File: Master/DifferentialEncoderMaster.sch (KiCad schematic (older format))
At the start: 52 parts, among them J1 RJ45_Shielded, J10 Conn_02x06_Top_Bottom, J11 Conn_02x06_Top_Bottom, J12 CAN_Header, J13 Conn_02x04_Top_Bottom, J2 Conn_01x06, J3 Conn_01x20, J4 Conn_01x12, J5 RJ45_Shielded, J6 RJ45_Shielded, J7 RJ45_Shielded, J8 Jumper, J9 Jumper, U1 SN75C1167, U2 SN75C1167, U3 ST26C32ABTR, U4 ST26C32ABTR, U5 ISO7760FDBQ, U6 ISO7761DBQ

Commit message: Big updates to master
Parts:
- removed J1, J5, J6, J7: RJ45_Shielded, Connector_RJ:RJ45_Amphenol_RJHSE538X, symbol Connector:RJ45_Shielded
- removed U5: ISO7760FDBQ, Package_SO:SSOP-16_3.9x4.9mm_P0.635mm, symbol Isolator:ISO7760FDBQ
- added C10, C11: 100nF, Capacitor_SMD:C_0603_1608Metric, symbol Device:C_Small
- added J1, J5: RJ45_Shielded_x2, Wetmelon:RJ45_RJSSE5380-02, symbol Wetmelon:RJ45_Shielded_x2
- added R19, R20: 0R, Resistor_SMD:R_0603_1608Metric, symbol Device:R_Small
- FB1, FB2: footprint (none) -> Inductor_SMD:L_0603_1608Metric
- J10: value Conn_02x06_Top_Bottom -> Encoder_0
- J11: value Conn_02x06_Top_Bottom -> Encoder_1
- J13: value Conn_02x04_Top_Bottom -> ISO_GPIO; footprint (none) -> Connector_Molex:Molex_Nano-Fit_105310-xx08_2x04_P2.50mm_Vertical
- J8, J9: footprint (none) -> Connector_PinHeader_2.54mm:PinHeader_1x02_P2.54mm_Vertical
- R17, R18: footprint (none) -> Resistor_SMD:R_0603_1608Metric
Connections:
- net IO_M0_A is gone; now on net M0_A: J10.2 (Pin_2), J10.4 (Pin_4), U3.3 (A_Out)
- net IO_M0_B is gone; now on net M0_B: J10.10 (Pin_10), J10.8 (Pin_8), U3.5 (B_Out)
- net IO_M0_Z is gone; now on net M0_Z: J10.11 (Pin_11), J10.7 (Pin_7), U3.11 (C_Out)
- net IO_M1_A is gone; now on net M1_A: J11.2 (Pin_2), J11.4 (Pin_4), U4.3 (A_Out)
- net IO_M1_B is gone; now on net M1_B: J11.10 (Pin_10), J11.8 (Pin_8), U4.5 (B_Out)
- net IO_M1_Z is gone; now on net M1_Z: J11.11 (Pin_11), J11.7 (Pin_7), U4.11 (C_Out)
- net +5V: now also C6.1, J10.1 (Pin_1), J10.5 (Pin_5), J11.1 (Pin_1), J11.5 (Pin_5), R17.2, R18.2, U3.16 (Vcc), U4.16 (Vcc), C10.1, C11.1, J1.15, J1.7, J5.15, J5.7
- net CLK_1+: now also J1.3
- net CLK_1-: now also J1.6
- net CLK_2+: now also J1.11
- net CLK_2-: now also J1.14
- net CSn_1: now also R19.1; no longer U1.4 (~RE)
- net CSn_1+: now also J1.1
- net CSn_1-: now also J1.2
- net CSn_2: now also R20.1; no longer U2.4 (~RE)
- net CSn_2+: now also J1.9
- net CSn_2-: now also J1.10
- net ENC0_A+: now also J5.1
- net ENC0_A-: now also J5.2
- net ENC0_B+: now also J5.3
- net ENC0_B-: now also J5.6
- net ENC0_Z+: now also J5.5
- net ENC0_Z-: now also J5.4
- net ENC1_A+: now also J5.9
- net ENC1_A-: now also J5.10
- net ENC1_B+: now also J5.11
- net ENC1_B-: now also J5.14
- net ENC1_Z+: now also J5.13
- net ENC1_Z-: now also J5.12
- net GNDD: now also C6.2, J8.2 (Pin_2), J9.2 (Pin_2), U3.4 (EN), U3.8 (GND), U4.4 (EN), U4.8 (GND), C10.2, C11.2, J1.16, J1.8, J1.SH, J1.SH, J5.16, J5.8, J5.SH, J5.SH
- net GPIO5: no longer J10.6 (Pin_6)
- net GPIO6: no longer J11.6 (Pin_6)
- net ISO_DIR_1: now also J13.3 (Pin_3), U6.3 (INB); no longer J13.4 (Pin_4), U6.4 (INC)
- net ISO_DIR_2: now also J13.7 (Pin_7); no longer J13.8 (Pin_8)
- net ISO_STEP_1: now also J13.4 (Pin_4); no longer J13.3 (Pin_3)
- net ISO_STEP_2: now also J13.8 (Pin_8), U6.4 (INC); no longer J13.7 (Pin_7), U6.3 (INB)
- net MISO_1+: now also J1.5
- net MISO_1-: now also J1.4
- net MISO_2+: now also J1.13
- net MISO_2-: now also J1.12
- removed net AGND: J10.12 (Pin_12), J11.12 (Pin_12), J3.7 (Pin_7)
- net AVCC: no longer names the net of J3.6 (Pin_6)
- removed net GND2: C6.2, C7.2, FB2.1, J13.2 (Pin_2), J8.2 (Pin_2), J9.2 (Pin_2), U3.4 (EN), U3.8 (GND), U4.4 (EN), U4.8 (GND), U6.8 (GND1)
- net MOSI: no longer names the net of J3.10 (Pin_10)
- net SWC: no longer names the net of J2.3 (Pin_3)
- net SWD: no longer names the net of J2.5 (Pin_5)
- removed net VDD: C6.1, C7.1, FB1.1, J10.1 (Pin_1), J10.5 (Pin_5), J11.1 (Pin_1), J11.5 (Pin_5), J13.1 (Pin_1), R17.2, R18.2, U3.16 (Vcc), U4.16 (Vcc), U6.1 (Vcc1)
- net ~RST: no longer names the net of J2.6 (Pin_6)
- new net: R19.2, U1.4 (~RE)
- new net: R20.2, U2.4 (~RE)
- new net GND1: C7.2, FB2.1, J13.2 (Pin_2), U6.8 (GND1)
- new net VDD1: C7.1, FB1.1, J13.1 (Pin_1), U6.1 (Vcc1)
- no-connect marks 12 -> 22
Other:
- note added: "AGND"
- note added: "AVCC"
- note added: "MOSI"
- note added: "RC Filters for Single-Ended SPI Signals\n10.6 MHz"
- note added: "SWC"
- note added: "SWD"
- note added: "~RST"
- note removed: "Incremental Encoder Isolator"
- note removed: "RC Filters for Single-Ended SPI Signals"
- moved on the sheet: C5, C7, C9, FB1, FB2, J10, J11, J12, J13, J2, J3, J4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

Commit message: Finish rev 1 layout
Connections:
- net ENC0_A+: now also J5.9; no longer J5.1
- net ENC0_A-: now also J5.10; no longer J5.2
- net ENC0_B+: now also J5.11; no longer J5.3
- net ENC0_B-: now also J5.14; no longer J5.6
- net ENC0_Z+: now also J5.13; no longer J5.5
- net ENC0_Z-: now also J5.12; no longer J5.4
- net ENC1_A+: now also J5.1; no longer J5.9
- net ENC1_A-: now also J5.2; no longer J5.10
- net ENC1_B+: now also J5.3; no longer J5.11
- net ENC1_B-: now also J5.6; no longer J5.14
- net ENC1_Z+: now also J5.5; no longer J5.13
- net ENC1_Z-: now also J5.4; no longer J5.12
- net GND1: now also J13.7 (Pin_7); no longer J13.2 (Pin_2)
- net ISO_DIR_1: now also J13.6 (Pin_6); no longer J13.3 (Pin_3)
- net ISO_DIR_2: now also J13.2 (Pin_2); no longer J13.7 (Pin_7)
- net ISO_STEP_1: now also J13.5 (Pin_5); no longer J13.4 (Pin_4)
- net ISO_STEP_2: now also J13.1 (Pin_1); no longer J13.8 (Pin_8)
- net ISO_UART_RX: now also J13.3 (Pin_3); no longer J13.6 (Pin_6)
- net ISO_UART_TX: now also J13.4 (Pin_4); no longer J13.5 (Pin_5)
- net VDD1: now also J13.8 (Pin_8); no longer J13.1 (Pin_1)
- removed net +3.3V: J2.2 (Pin_2), J3.1 (Pin_1), J4.1 (Pin_1), J4.7 (Pin_7)
- no-connect marks 22 -> 26
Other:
- note added: "+3.3V"
- moved on the sheet: J5A, J5B
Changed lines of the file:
@@
 Text Label 12400 5200 2    50   ~ 0
 GPIO8
-$Comp
-L Connector_Generic:Conn_02x04_Top_Bottom J13
-U 1 1 60674364
-P 11500 6900
-F 0 "J13" H 11550 7217 50  0000 C CNN
-F 1 "ISO_GPIO" H 11550 7126 50  0000 C CNN
-F 2 "Connector_Molex:Molex_Nano-Fit_105310-xx08_2x04_P2.50mm_Vertical" H 11500 6900 50  0001 C CNN
-F 3 "~" H 11500 6900 50  0001 C CNN
-	1    11500 6900
-	1    0    0    -1
-$EndComp
-Wire Wire Line
-	10800 6800 11300 6800
 Text Label 10800 6900 0    50   ~ 0
 GND1
-Wire Wire Line
-	10800 6900 11300 6900
 Text Label 10800 7100 0    50   ~ 0
 ISO_STEP_1
-Wire Wire Line
-	10800 7000 11300 7000
 Text Label 10800 7000 0    50   ~ 0
 ISO_DIR_1
-Wire Wire Line
-	10800 7100 11300 7100
 Text Label 12400 6800 2    50   ~ 0
 ISO_UART_TX
@@
 	14550 4700 14850 4700
 Wire Wire Line
-	14550 4600 14850 4600
-Wire Wire Line
 	14550 4500 14850 4500
 Wire Wire Line
@@
 Wire Wire Line
 	14550 4100 14850 4100
-Wire Wire Line
-	14550 4000 14850 4000
 Text Label 14550 5100 0    50   ~ 0
 GNDD
@@
 Text Label 14550 4700 0    50   ~ 0
 +5V
-Text Label 14550 4600 0    50   ~ 0
-+3.3V
 Text Label 14550 4500 0    50   ~ 0
 GNDD
@@
 Text Label 14550 4100 0    50   ~ 0
 +5V
-Text Label 14550 4000 0    50   ~ 0
-+3.3V
 $Comp
 L Connector_Generic:Conn_01x12 J4
@@
 Text Label 13250 4100 0    50   ~ 0
 GNDD
-Text Label 13250 4000 0    50   ~ 0
-+3.3V
-Wire Wire Line
-	13600 4000 13250 4000
 $Comp
 L Connector_Generic:Conn_01x20 J3
@@
 Text Label 14500 5400 0    50   ~ 0
 +5V
-Text Label 14500 5500 0    50   ~ 0
-+3.3V
 Text Label 14500 5700 0    50   ~ 0
 GNDD
 Wire Wire Line
 	14500 5400 14850 5400
-Wire Wire Line
-	14500 5500 14850 5500
 Wire Wire Line
 	14500 5700 14850 5700
@@
 L Wetmelon:RJ45_Shielded_x2 J5
 U 1 1 5FB86974
+P 6550 5200
+F 0 "J5" H 6607 5867 50  0000 C CNN
+F 1 "RJ45_Shielded_x2" H 6607 5776 50  0000 C CNN
+F 2 "Wetmelon:RJ45_RJSSE5380-02" V 6550 5225 50  0001 C CNN
+F 3 "~" V 6550 5225 50  0001 C CNN
+	1    6550 5200
+	-1   0    0    -1
+$EndComp
+$Comp
+L Wetmelon:RJ45_Shielded_x2 J5
+U 2 1 5FB876DB
 P 6550 2550
 F 0 "J5" H 6607 3217 50  0000 C CNN
@@
 F 2 "Wetmelon:RJ45_RJSSE5380-02" V 6550 2575 50  0001 C CNN
 F 3 "~" V 6550 2575 50  0001 C CNN
-	1    6550 2550
-	-1   0    0    -1
-$EndComp
-$Comp
-L Wetmelon:RJ45_Shielded_x2 J5
-U 2 1 5FB876DB
-P 6550 5200
-F 0 "J5" H 6607 5867 50  0000 C CNN
-F 1 "RJ45_Shielded_x2" H 6607 5776 50  0000 C CNN
-F 2 "Wetmelon:RJ45_RJSSE5380-02" V 6550 5225 50  0001 C CNN
-F 3 "~" V 6550 5225 50  0001 C CNN
-	2    6550 5200
+	2    6550 2550
 	-1   0    0    -1
 $EndComp
@@
 Text Label 10500 4900 0    50   ~ 0
 ISO_STEP_1
+Wire Wire Line
+	10800 7100 11300 7100
+Wire Wire Line
+	10800 6800 11300 6800
+Wire Wire Line
+	10800 6900 11300 6900
+Wire Wire Line
+	10800 7000 11300 7000
+$Comp
+L Connector_Generic:Conn_02x04_Top_Bottom J13
+U 1 1 60674364
+P 11600 7000
+F 0 "J13" H 11650 7317 50  0000 C CNN
+F 1 "ISO_GPIO" H 11650 7226 50  0000 C CNN
+F 2 "Connector_Molex:Molex_Nano-Fit_105310-xx08_2x04_P2.50mm_Vertical" H 11600 7000 50  0001 C CNN
+F 3 "~" H 11600 7000 50  0001 C CNN
+	1    11600 7000
+	-1   0    0    1
+$EndComp
+Text Notes 13250 4000 0    50   ~ 0
++3.3V
+NoConn ~ 13600 4000
+Text Notes 14550 4000 0    50   ~ 0
++3.3V
+Text Notes 14550 4600 0    50   ~ 0
++3.3V
+Text Notes 14500 5500 0    50   ~ 0
++3.3V
+NoConn ~ 14850 4000
+NoConn ~ 14850 4600
+NoConn ~ 14850 5500
 $EndSCHEMATC

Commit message: Odrive side TSSOP->SSOP
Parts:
- U1, U2: footprint Package_SO:TSSOP-16_4.4x5mm_P0.65mm -> Package_SO:SSOP-16_5.3x6.2mm_P0.65mm
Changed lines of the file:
@@
 F 0 "U2" H 2900 5900 50  0000 C CNN
 F 1 "SN75C1167" H 3050 5800 50  0000 C CNN
-F 2 "Package_SO:TSSOP-16_4.4x5mm_P0.65mm" H 3400 5850 50  0001 C CNN
+F 2 "Package_SO:SSOP-16_5.3x6.2mm_P0.65mm" H 3400 5850 50  0001 C CNN
 F 3 "https://www.ti.com/lit/ds/symlink/sn65c1168.pdf" H 3400 5850 50  0001 C CNN
 	1    3400 4950
@@
 F 0 "U1" H 2900 3150 50  0000 C CNN
 F 1 "SN75C1167" H 3050 3050 50  0000 C CNN
-F 2 "Package_SO:TSSOP-16_4.4x5mm_P0.65mm" H 3400 3100 50  0001 C CNN
+F 2 "Package_SO:SSOP-16_5.3x6.2mm_P0.65mm" H 3400 3100 50  0001 C CNN
 F 3 "https://www.ti.com/lit/ds/symlink/sn65c1168.pdf" H 3400 3100 50  0001 C CNN
 	1    3400 2200

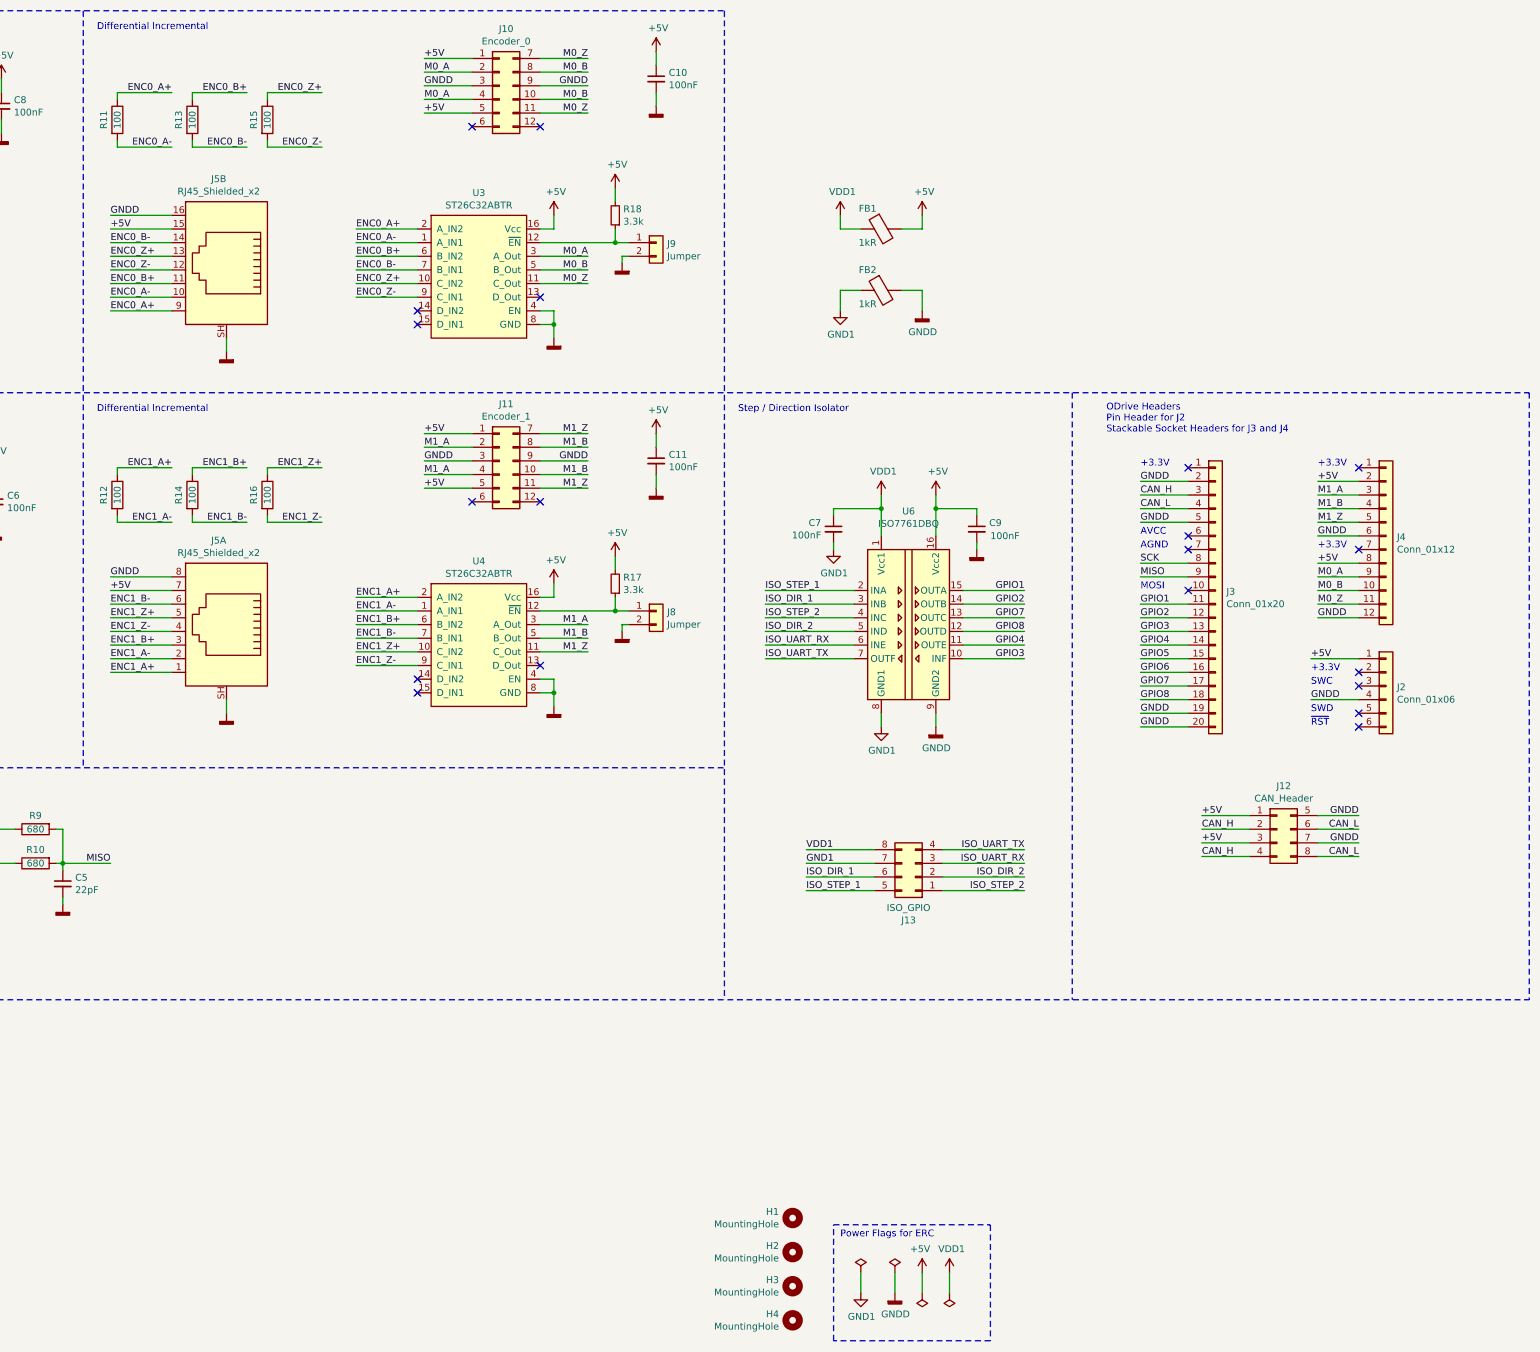
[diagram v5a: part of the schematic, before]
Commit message: Remove differential encoder half
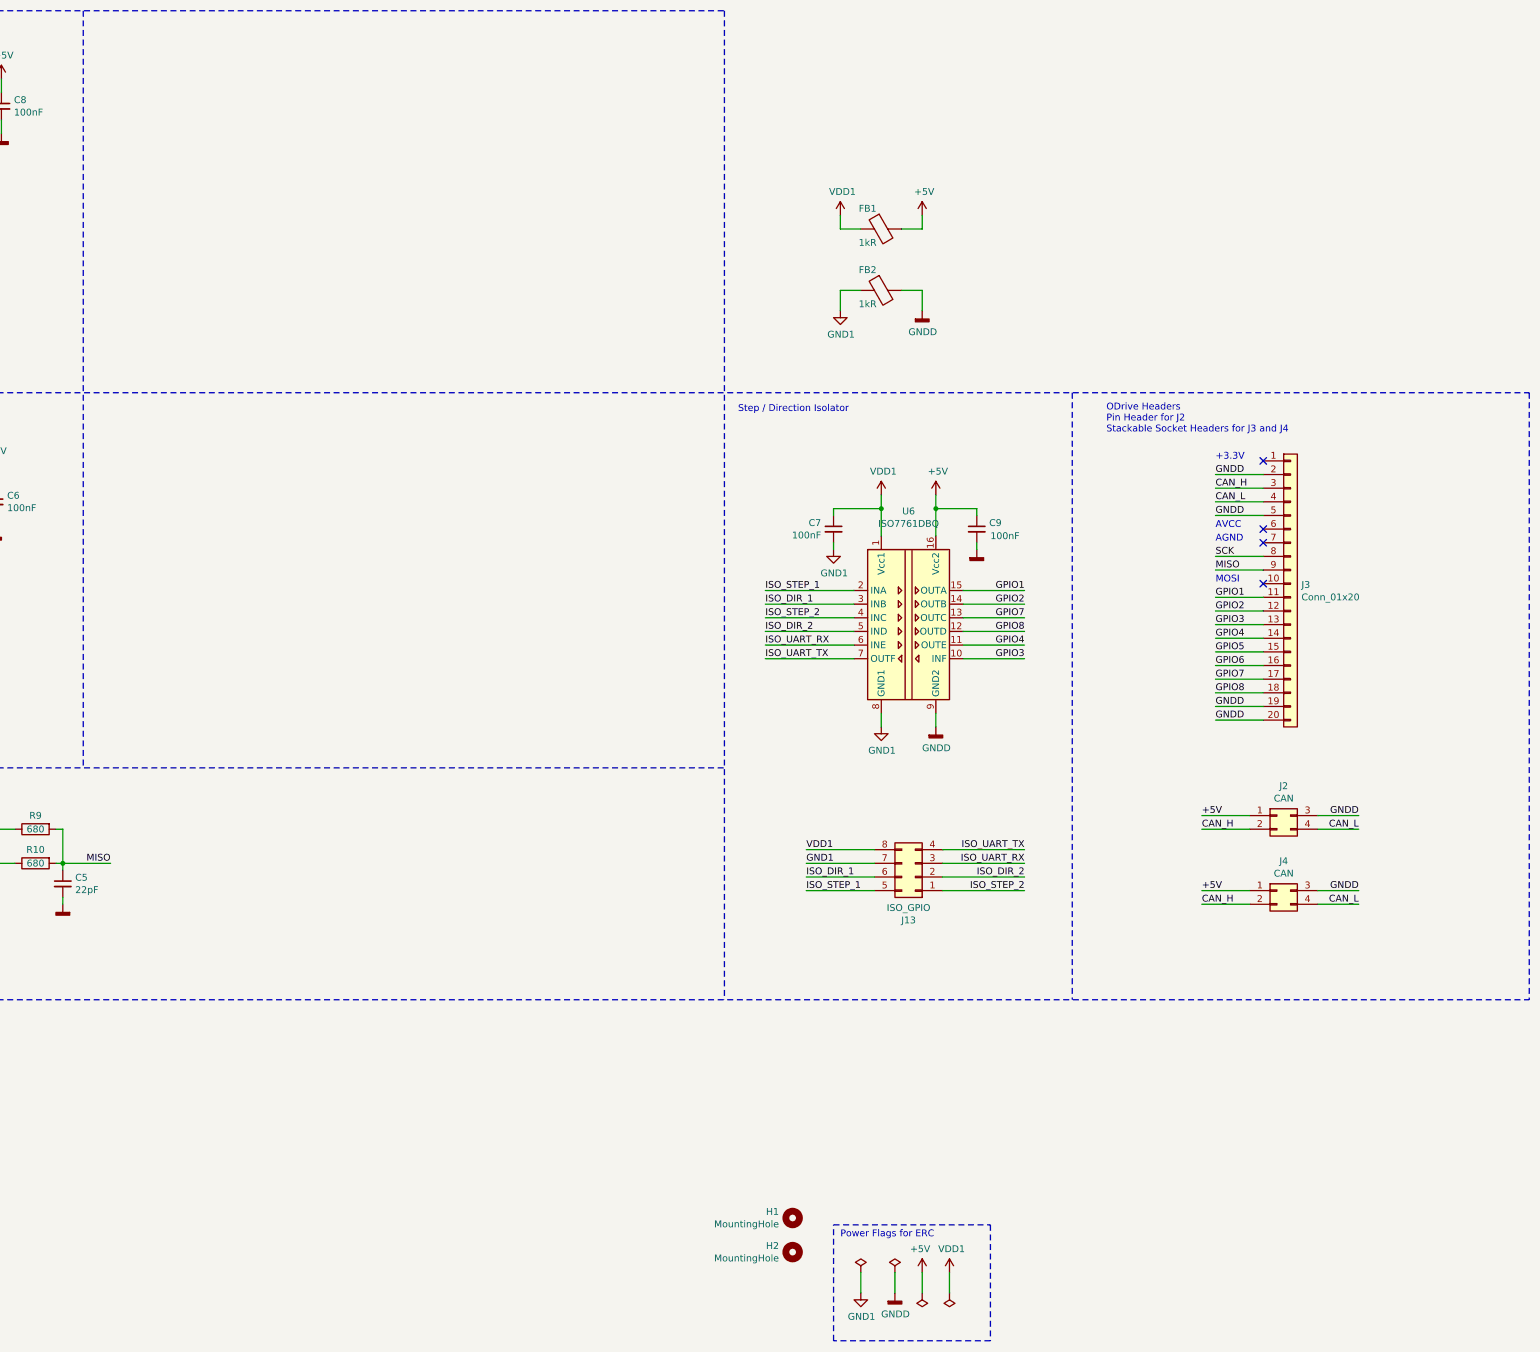
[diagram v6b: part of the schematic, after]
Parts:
- removed C10, C11: 100nF, Capacitor_SMD:C_0603_1608Metric, symbol Device:C_Small
- removed H3, H4: MountingHole, MountingHole:MountingHole_3.2mm_M3, symbol Mechanical:MountingHole
- removed J10: Encoder_0, Connector_Molex:Molex_Nano-Fit_105310-xx12_2x06_P2.50mm_Vertical, symbol Connector_Generic:Conn_02x06_Top_Bottom
- removed J11: Encoder_1, Connector_Molex:Molex_Nano-Fit_105310-xx12_2x06_P2.50mm_Vertical, symbol Connector_Generic:Conn_02x06_Top_Bottom
- removed J12: CAN_Header, Connector_Molex:Molex_Nano-Fit_105310-xx08_2x04_P2.50mm_Vertical, symbol Connector_Generic:Conn_02x04_Top_Bottom
- removed J2: Conn_01x06, Connector_PinSocket_2.54mm:PinSocket_1x06_P2.54mm_Vertical, symbol Connector_Generic:Conn_01x06
- removed J4: Conn_01x12, Connector_PinSocket_2.54mm:PinSocket_1x12_P2.54mm_Vertical, symbol Connector_Generic:Conn_01x12
- removed J5: RJ45_Shielded_x2, Wetmelon:RJ45_RJSSE5380-02, symbol Wetmelon:RJ45_Shielded_x2
- removed J8, J9: Jumper, Connector_PinHeader_2.54mm:PinHeader_1x02_P2.54mm_Vertical, symbol Connector_Generic:Conn_01x02
- removed R11, R12, R13, R14, R15, R16: 100, Resistor_SMD:R_0603_1608Metric, symbol Device:R
- removed R17, R18: 3.3k, Resistor_SMD:R_0603_1608Metric, symbol Device:R_Small
- removed U3, U4: ST26C32ABTR, Package_SO:TSSOP-16_4.4x5mm_P0.65mm, symbol Wetmelon:ST26C32ABTR
- added J2, J4: CAN, Connector_Molex:Molex_Nano-Fit_105310-xx04_2x02_P2.50mm_Vertical, symbol Connector_Generic:Conn_02x02_Top_Bottom
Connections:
- net +5V: now also J2.1 (Pin_1), J4.1 (Pin_1)
- net CAN_H: now also J2.2 (Pin_2), J4.2 (Pin_2)
- net CAN_L: now also J2.4 (Pin_4), J4.4 (Pin_4)
- net GNDD: now also J2.3 (Pin_3), J4.3 (Pin_3)
- no-connect marks 26 -> 10
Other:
- note removed: "Differential Incremental"
- note removed: "SWC"
- note removed: "SWD"
- note removed: "~RST"
- moved on the sheet: J3

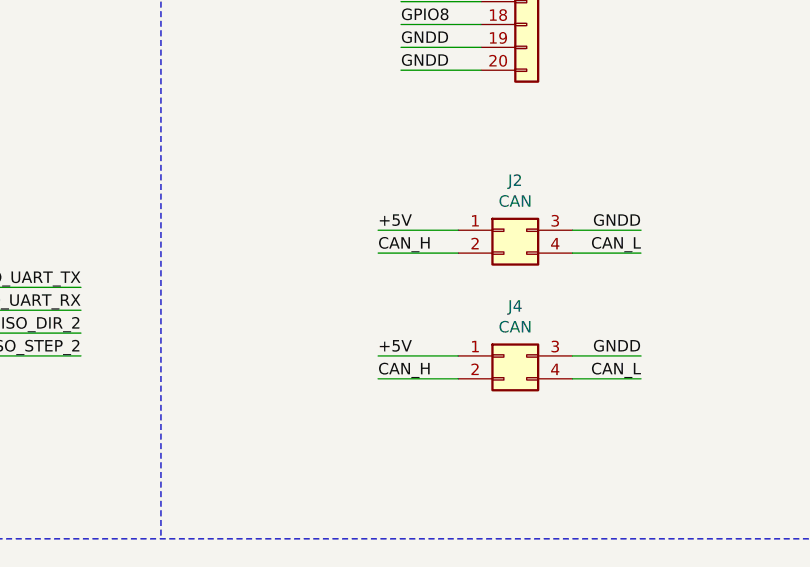
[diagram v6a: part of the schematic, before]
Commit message: Optimize layout - remove ~ 15% of vias
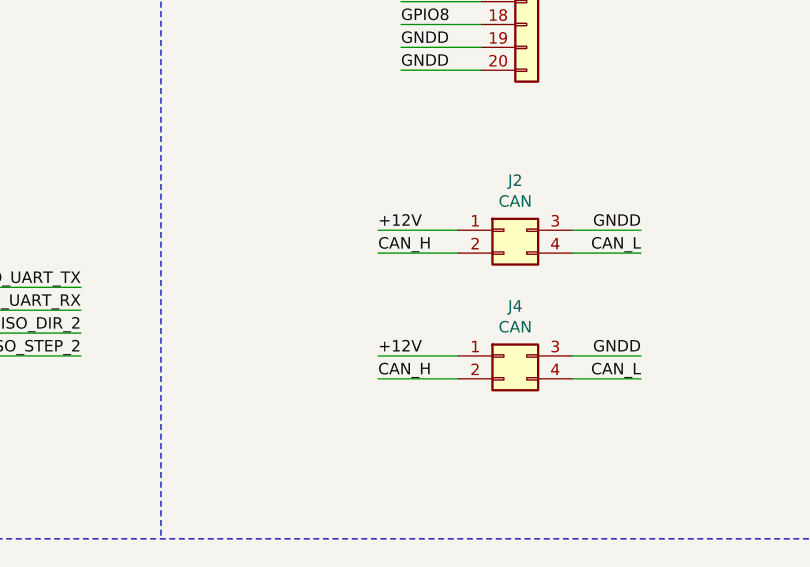
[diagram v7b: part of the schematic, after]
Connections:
- net +5V: no longer J2.1 (Pin_1), J4.1 (Pin_1)
- new net +12V: J2.1 (Pin_1), J4.1 (Pin_1)
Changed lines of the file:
@@
 GNDD
 Text Label 13700 7100 0    50   ~ 0
-+5V
++12V
 Wire Wire Line
 	14850 6550 14550 6550
@@
 GNDD
 Text Label 13700 6550 0    50   ~ 0
-+5V
++12V
 Wire Notes Line
 	5500 650  5500 6200
